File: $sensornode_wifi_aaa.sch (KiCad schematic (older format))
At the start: 31 parts, among them K1 ICSP, K2 USB, K3 AD-HOC, SW1 uC_RESET, SW2 WiFi_RESET, U1 MCP1640, U2 PIC18F2XJ53, U3 RN-171, X1 CRYSTAL_4P

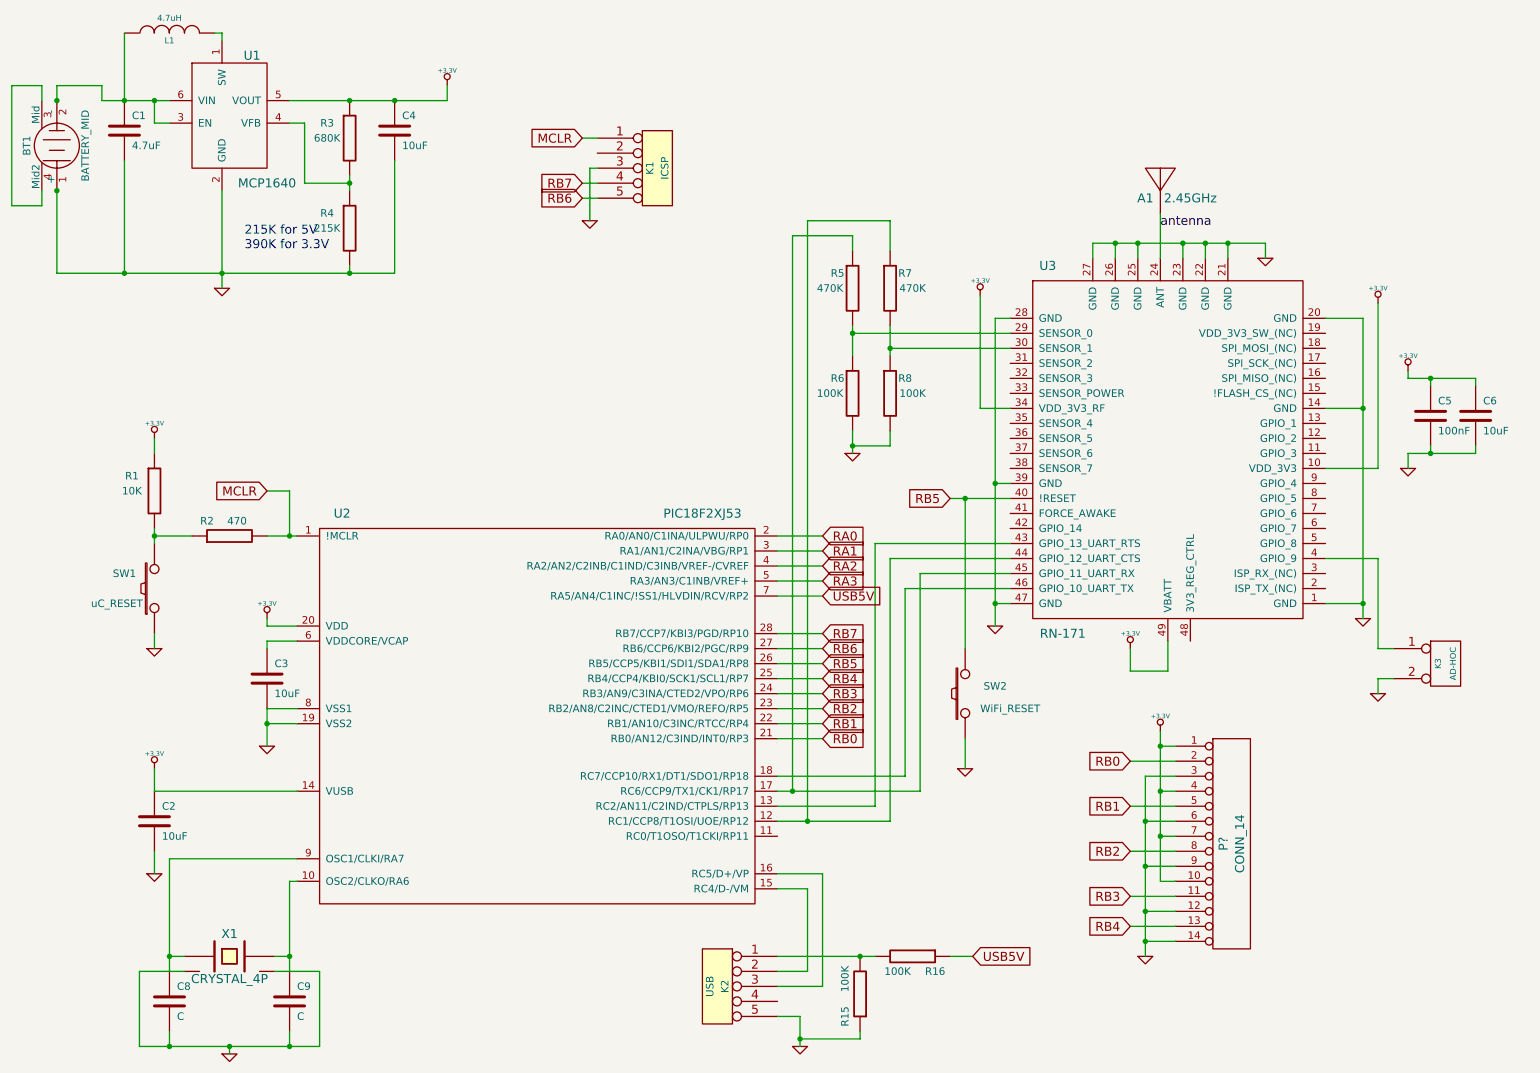
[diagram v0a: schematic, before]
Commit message: new layout, changed connectors to 0.1in
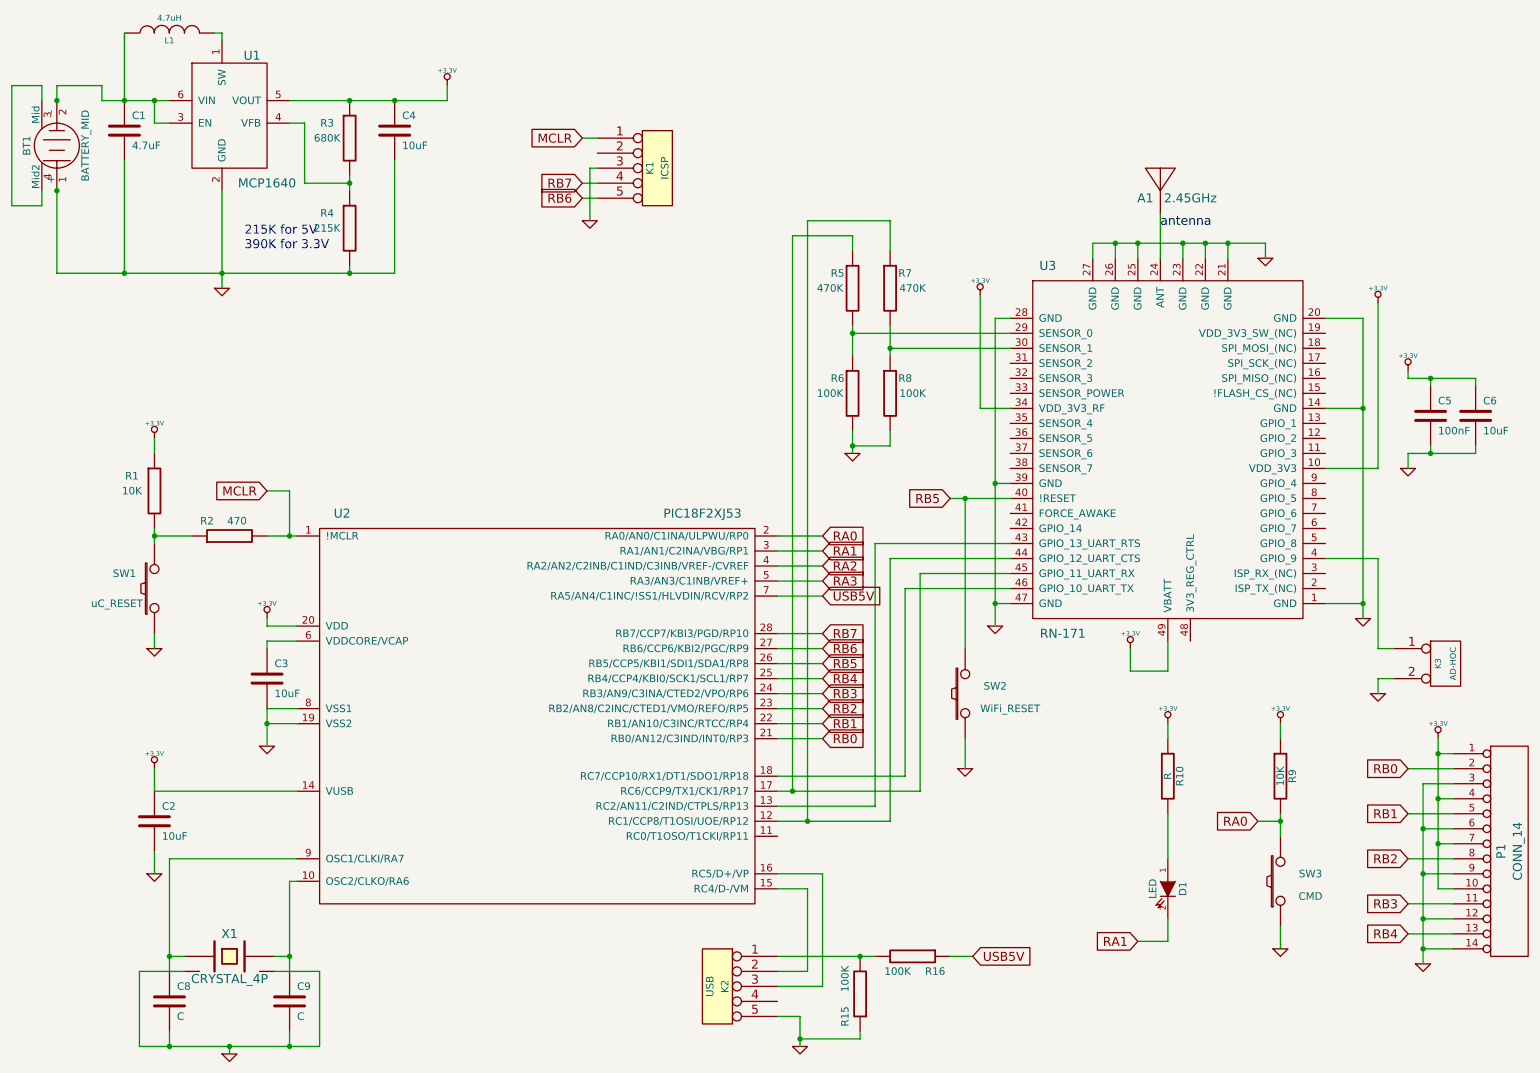
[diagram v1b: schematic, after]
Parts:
- added D1: LED, symbol LED
- added R10: R, symbol R
- added R9: 10K, symbol R
- added SW3: CMD, symbol SW_PUSH
- gave numbers to parts that had none: 1
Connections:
- net +3.3V: now also R10.1, R9.1
- net GND: now also SW3.1
- net RA0: now also R9.2, SW3.2
- net RA1: now also D1.2 (K)
- new net: D1.1 (A), R10.2
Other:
- moved on the sheet: P1
